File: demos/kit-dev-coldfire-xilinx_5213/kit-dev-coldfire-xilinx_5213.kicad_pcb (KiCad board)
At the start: 4 copper layers, 157.5 x 91.4 mm, 162 parts, among them J1 JACK_2P, P1 CONN_6, P3 CONN_2X2, P4 CONN_20X2, Q1 3906, SW1 SW_PUSH, SW2 SW_PUSH, U1 MCF5213-LQFP100, U2 74AHC1G14, U3 MAX202, U4 74HC125, U5 MAX202, U7 PCA82C251, U8 MAX202, U9 XCR3256-TQ144, Y1 8MHz

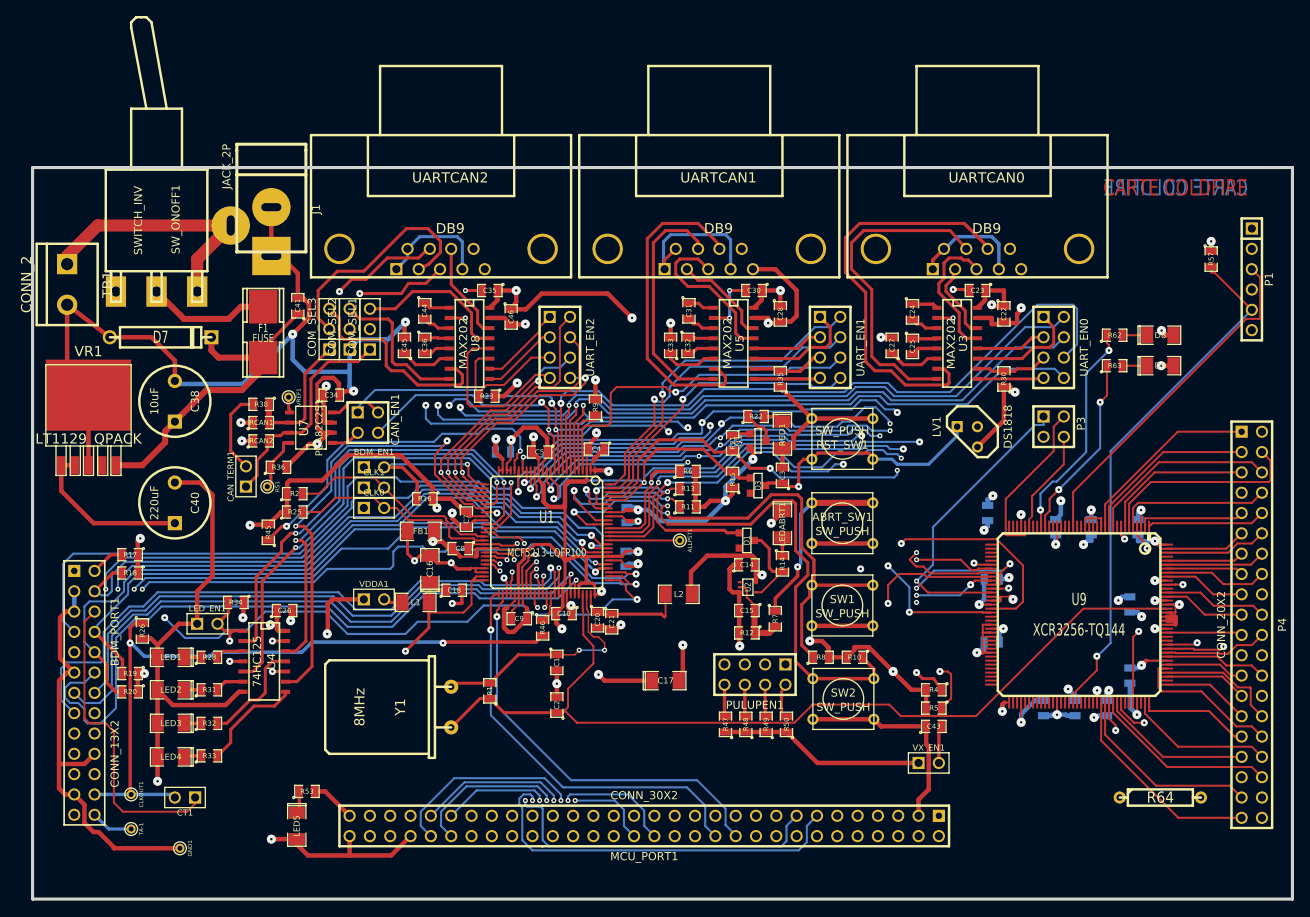
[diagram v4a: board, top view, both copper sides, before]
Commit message: 3d viewer: minor code cleaning (remove useless #include ) dialog_track_via_size: set minimal size  and make dialog resizable. Update demo file.
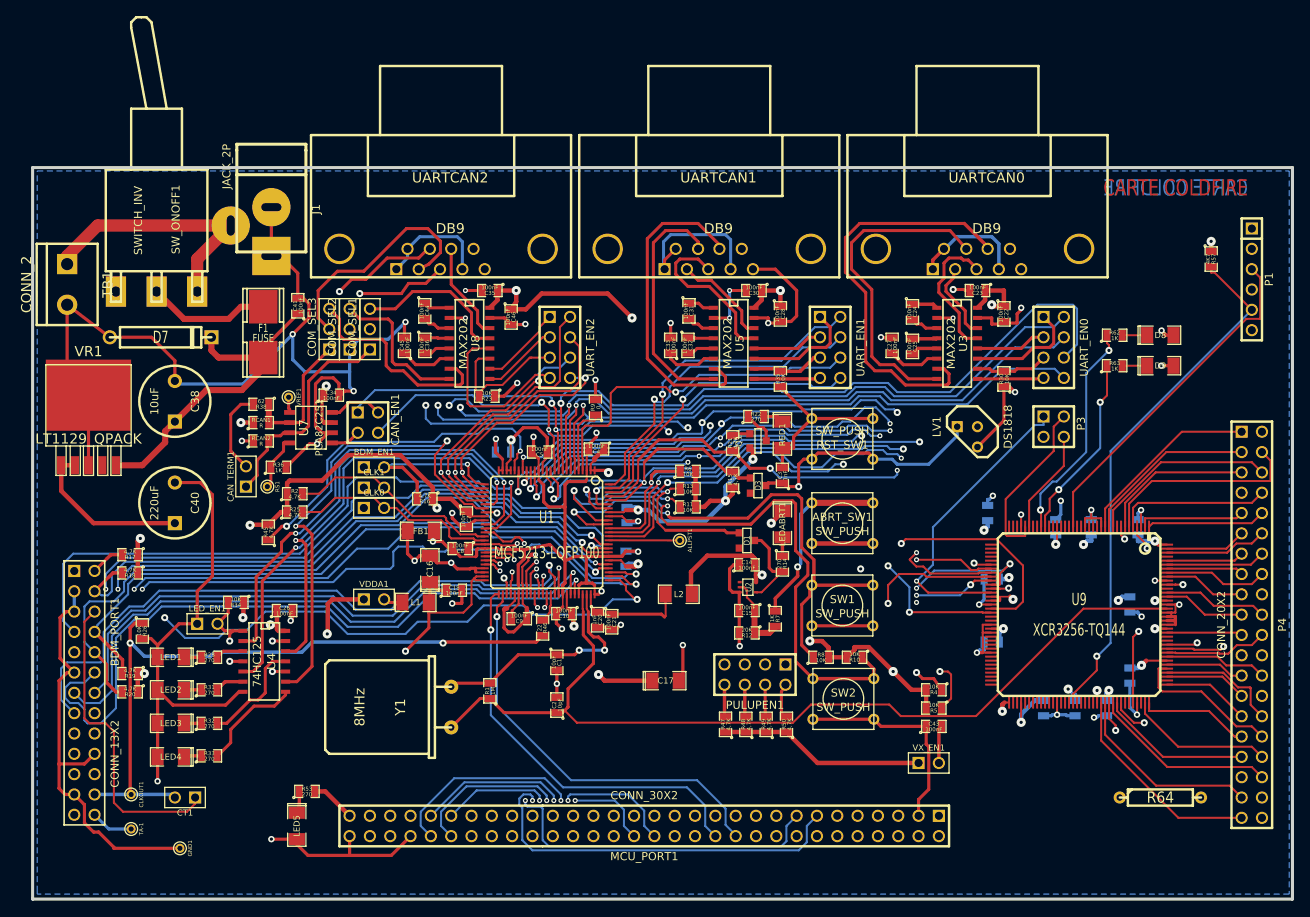
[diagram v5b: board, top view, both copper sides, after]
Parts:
- ABRT_SW1, RST_SW1, SW1, SW2: footprint SW_PUSH_SMALL -> discret:SW_PUSH_SMALL
- ALLPST1, CLKOUT1, GND1, RS1, TA-1, VREF1: footprint PINTST -> connect:PINTST
- BDM_EN1, CAN_TERM1, CLK0, CLK1, CT1, LED_EN1, VDDA1, VX_EN1: footprint PIN_ARRAY_2X1 -> pin_array:PIN_ARRAY_2X1
- BDM_PORT1: footprint pin_array_13x2 -> pin_array:pin_array_13x2
- C1, C10, C11, C12, C14, C15, C18, C2, C20, C21, C22, C23, C24, C25, C26, C27, C28, C3, C30, C31, C32, C33, C34, C35, C36, C4, C41, C43, C44, C45, C46, C5, C51, C52, C53, C54, C55, C56, C57, C58, C59, C6, C60, C61, C7, C8, C9, R1, R10, R11, R12, R13, R14, R15, R16, R17, R18, R19, R2, R20, R21, R22, R23, R25, R26, R28, R30, R31, R32, R33, R34, R35, R36, R38, R4, R45, R46, R47, R48, R49, R5, R50, R53, R57, R6, R62, R63, R7, R8, R9, RCAN1, RCAN2: footprint SM0805 -> lib_smd:SM0805
- C16, C17, D8, D9, LED1, LED2, LED3, LED4, LED5, LEDABRT1, RED1: footprint SM1206POL -> lib_smd:SM1206POL
- C38, C40: footprint C2V8 -> discret:C2V8
- CAN_EN1, P3: footprint PIN_ARRAY_2X2 -> pin_array:PIN_ARRAY_2X2
- COM_SEL1, COM_SEL2, COM_SEL3: footprint PIN_ARRAY_3X1 -> pin_array:PIN_ARRAY_3X1
- D1, D3: footprint ST23AK#1 -> lib_smd:ST23AK#1
- D7: footprint D5 -> discret:D5
- F1: footprint FSUPCMS -> lib_smd:FSUPCMS
- FB1, L1, L2: footprint SM1206 -> lib_smd:SM1206
- J1: footprint JACK_ALIM -> connect:JACK_ALIM
- LV1: footprint TO92-INVERT -> discret:TO92-INVERT
- MCU_PORT1: footprint PIN_ARRAY_30X2 -> pin_array:PIN_ARRAY_30X2
- P1: footprint PIN_ARRAY-6X1 -> pin_array:PIN_ARRAY-6X1
- P4: footprint PIN_ARRAY_20X2 -> pin_array:PIN_ARRAY_20X2
- PULUPEN1, UART_EN0, UART_EN1, UART_EN2: footprint pin_array_4x2 -> pin_array:pin_array_4x2
- Q1: footprint SOT23EBC -> lib_smd:SOT23EBC
- R64: footprint R4 -> discret:R4
- SW_ONOFF1: footprint SW_SPDT -> discret:SW_SPDT
- TB1: footprint bornier2 -> connect:bornier2
- U1: footprint VQFP100 -> lib_smd:VQFP100
- U2: footprint SOT353 -> lib_smd:SOT353
- U3, U5, U8: footprint SO16E -> lib_smd:SO16E
- U4: footprint SO14E -> lib_smd:SO14E
- U7: footprint SO8E -> lib_smd:SO8E
- U9: footprint TQFP144 -> lib_smd:TQFP144
- UARTCAN0, UARTCAN1, UARTCAN2: footprint DB9FC -> connect:DB9FC
- VR1: footprint DPAK5 -> lib_smd:DPAK5
- Y1: footprint HC-18UH -> discret:HC-18UH
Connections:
- BDM_PORT1 pad 1: Net-(BDM_PORT1-Pad1) -> (no net)
- BDM_PORT1 pad 21: Net-(BDM_PORT1-Pad21) -> (no net)
- BDM_PORT1 pad 22: Net-(BDM_PORT1-Pad22) -> (no net)
- SW_ONOFF1 pad 1: Net-(SW_ONOFF1-Pad1) -> (no net)
- U9 pad 102: Net-(U9-Pad102) -> (no net)
- U9 pad 103: Net-(U9-Pad103) -> (no net)
- U9 pad 106: Net-(U9-Pad106) -> (no net)
- U9 pad 110: Net-(U9-Pad110) -> (no net)
- U9 pad 120: Net-(U9-Pad120) -> (no net)
- U9 pad 121: Net-(U9-Pad121) -> (no net)
- U9 pad 133: Net-(U9-Pad133) -> (no net)
- U9 pad 14: Net-(U9-Pad14) -> (no net)
- U9 pad 141: Net-(U9-Pad141) -> (no net)
- U9 pad 15: Net-(U9-Pad15) -> (no net)
- U9 pad 16: Net-(U9-Pad16) -> (no net)
- U9 pad 18: Net-(U9-Pad18) -> (no net)
- U9 pad 19: Net-(U9-Pad19) -> (no net)
- U9 pad 21: Net-(U9-Pad21) -> (no net)
- U9 pad 22: Net-(U9-Pad22) -> (no net)
- U9 pad 23: Net-(U9-Pad23) -> (no net)
- U9 pad 25: Net-(U9-Pad25) -> (no net)
- U9 pad 26: Net-(U9-Pad26) -> (no net)
- U9 pad 29: Net-(U9-Pad29) -> (no net)
- U9 pad 30: Net-(U9-Pad30) -> (no net)
- U9 pad 34: Net-(U9-Pad34) -> (no net)
- U9 pad 35: Net-(U9-Pad35) -> (no net)
- U9 pad 36: Net-(U9-Pad36) -> (no net)
- U9 pad 37: Net-(U9-Pad37) -> (no net)
- U9 pad 38: Net-(U9-Pad38) -> (no net)
- U9 pad 39: Net-(U9-Pad39) -> (no net)
- U9 pad 40: Net-(U9-Pad40) -> (no net)
- U9 pad 41: Net-(U9-Pad41) -> (no net)
- U9 pad 55: Net-(U9-Pad55) -> (no net)
- U9 pad 56: Net-(U9-Pad56) -> (no net)
- U9 pad 60: Net-(U9-Pad60) -> (no net)
- U9 pad 61: Net-(U9-Pad61) -> (no net)
- U9 pad 62: Net-(U9-Pad62) -> (no net)
- U9 pad 63: Net-(U9-Pad63) -> (no net)
- U9 pad 65: Net-(U9-Pad65) -> (no net)
- U9 pad 66: Net-(U9-Pad66) -> (no net)
- U9 pad 67: Net-(U9-Pad67) -> (no net)
- U9 pad 68: Net-(U9-Pad68) -> (no net)
- U9 pad 69: Net-(U9-Pad69) -> (no net)
- U9 pad 70: Net-(U9-Pad70) -> (no net)
- U9 pad 71: Net-(U9-Pad71) -> (no net)
- U9 pad 72: Net-(U9-Pad72) -> (no net)
- U9 pad 74: Net-(U9-Pad74) -> (no net)
- U9 pad 75: Net-(U9-Pad75) -> (no net)
- U9 pad 77: Net-(U9-Pad77) -> (no net)
- U9 pad 78: Net-(U9-Pad78) -> (no net)
- U9 pad 79: Net-(U9-Pad79) -> (no net)
- U9 pad 80: Net-(U9-Pad80) -> (no net)
- U9 pad 81: Net-(U9-Pad81) -> (no net)
- U9 pad 82: Net-(U9-Pad82) -> (no net)
- U9 pad 83: Net-(U9-Pad83) -> (no net)
- U9 pad 84: Net-(U9-Pad84) -> (no net)
- U9 pad 86: Net-(U9-Pad86) -> (no net)
- U9 pad 87: Net-(U9-Pad87) -> (no net)
- U9 pad 88: Net-(U9-Pad88) -> (no net)
- U9 pad 9: Net-(U9-Pad9) -> (no net)
- U9 pad 90: Net-(U9-Pad90) -> (no net)
- U9 pad 91: Net-(U9-Pad91) -> (no net)
- U9 pad 92: Net-(U9-Pad92) -> (no net)
- U9 pad 93: Net-(U9-Pad93) -> (no net)
- U9 pad 94: Net-(U9-Pad94) -> (no net)
- UARTCAN0 pad 9: Net-(UARTCAN0-Pad9) -> (no net)
- UARTCAN1 pad 9: Net-(UARTCAN1-Pad9) -> (no net)
- UARTCAN2 pad 9: Net-(UARTCAN2-Pad9) -> (no net)
- VR1 pad 4: Net-(VR1-Pad4) -> (no net)
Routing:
- net GNDA: track 92.3 -> 62.7 mm
- net VDD: track 981.5 -> 983.5 mm
- net /DSI: track 81.7 -> 80.2 mm
- net /PST0: track 81.2 -> 82.1 mm
- net /PST2: track 78.5 -> 79.0 mm
- added copper zone on 3.3V_layer, net +3.3V
- added copper zone on B.Cu, net GND
- removed copper zone on 3.3V_layer, net VDD
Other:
- net class Default: clearance 0.16 -> 0.15; trace_width 0.25 -> 0.2; via_dia 0.635 -> 0.6; via_drill 0.3 -> 0.4
- net class POWER added: clearance 0.15, trace_width 0.4, via_dia 0.8, via_drill 0.4
- net class power removed
- rule trace_clearance: 0.16 -> 0.15
- rule trace_min: 0.18 -> 0.19812
- rule via_min_drill: 0.2 -> 0.4
- rule via_min_size: 0.45 -> 0.5
